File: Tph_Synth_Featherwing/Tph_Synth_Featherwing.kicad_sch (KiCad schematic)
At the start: 3 parts, among them J1 AudioJack3, J2 Conn_01x04

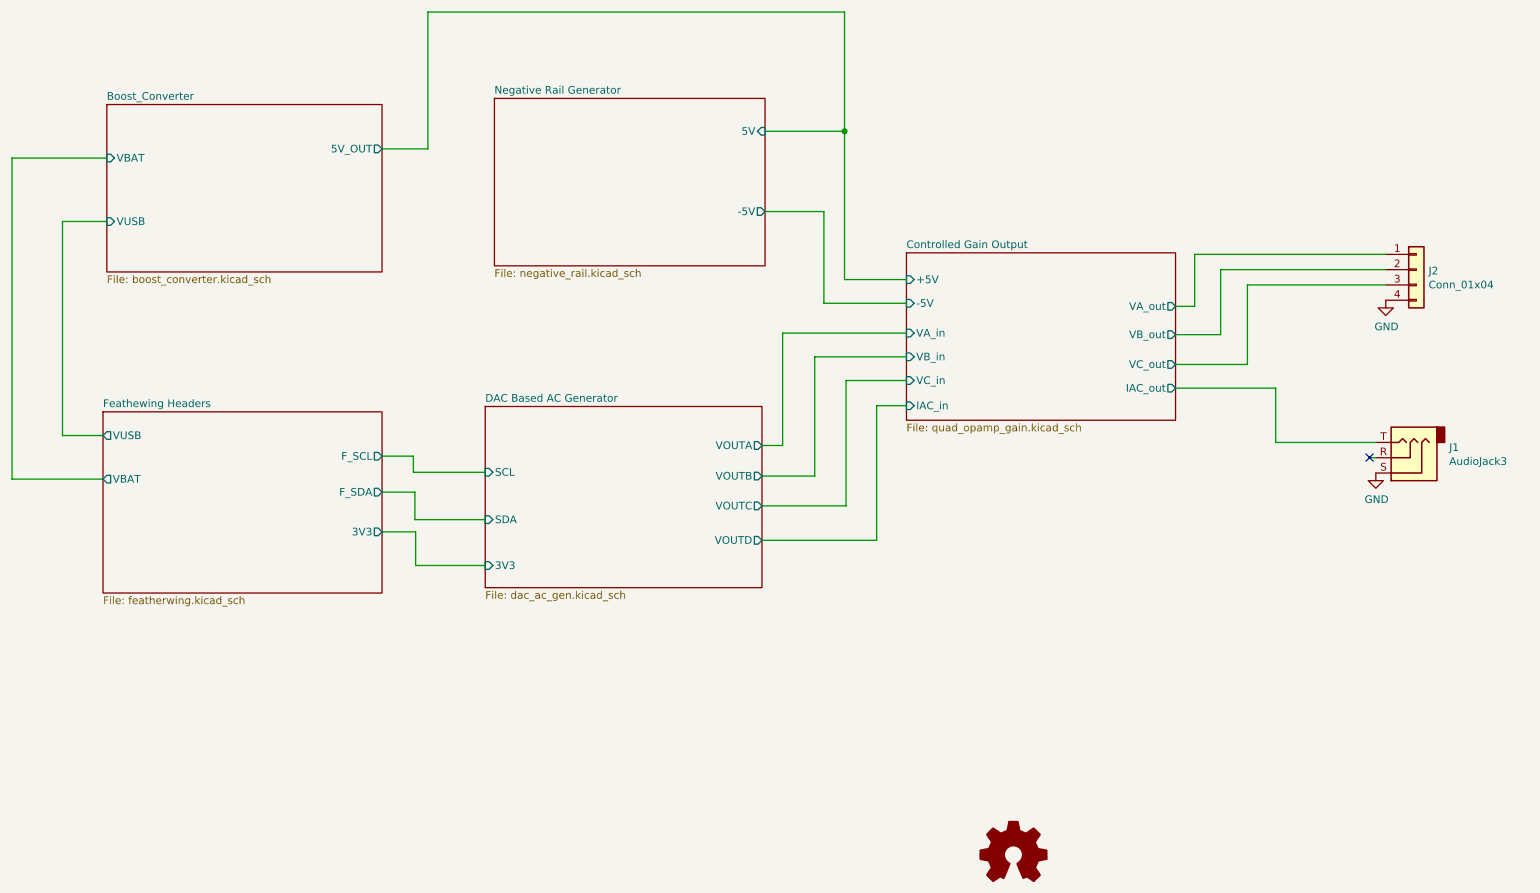
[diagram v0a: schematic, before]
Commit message: Upgrade design to KiCad 10; clear ERC and DRC violations
Co-authored-by: Copilot <223556219+Copilot@users.noreply.github.com>
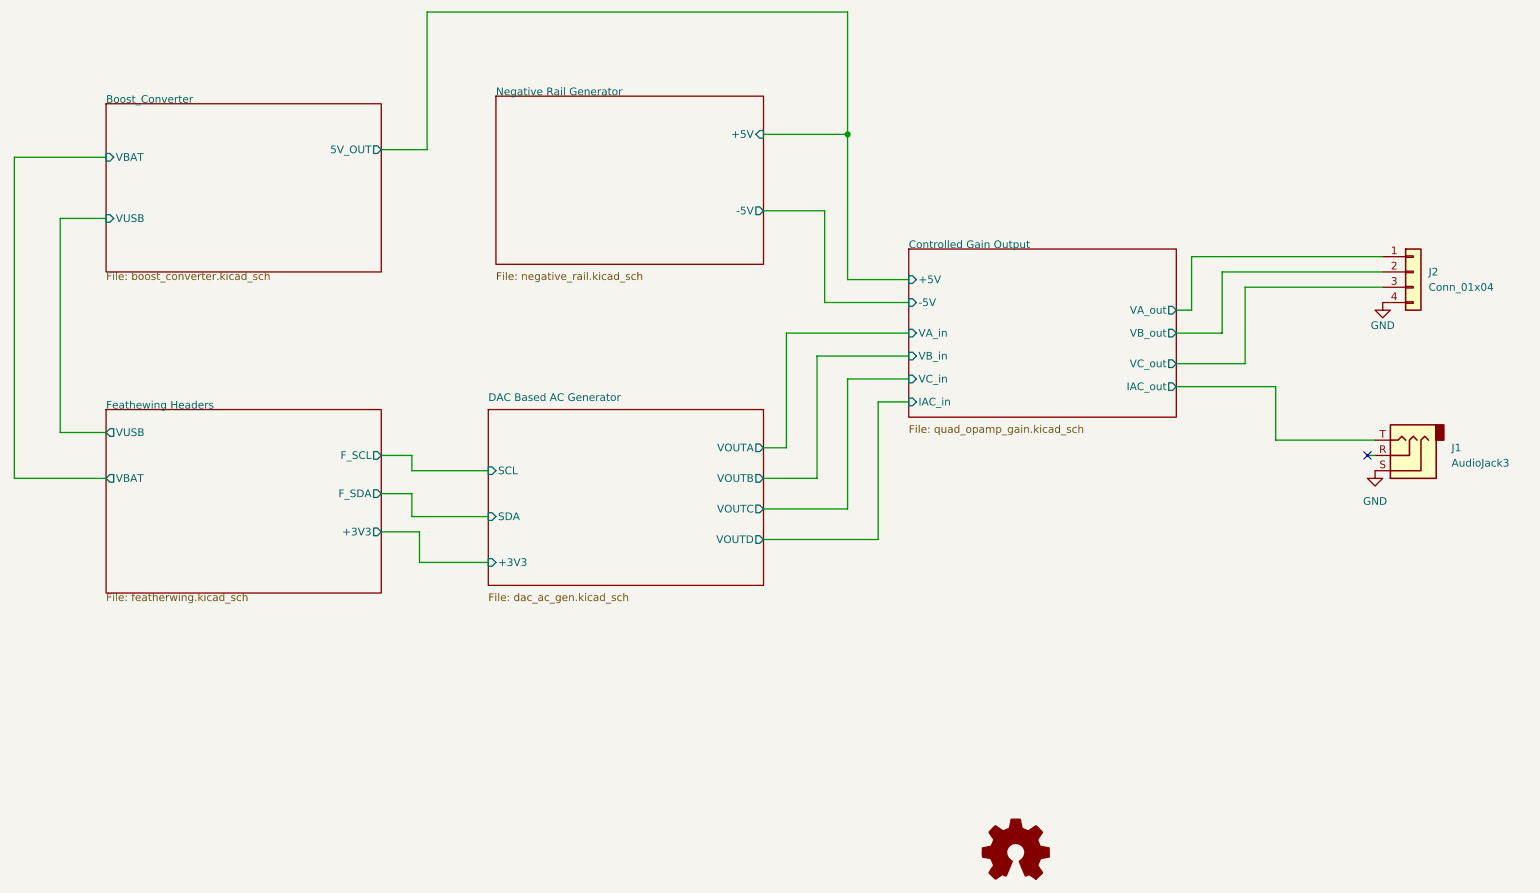
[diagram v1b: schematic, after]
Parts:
- J1: symbol Connector:AudioJack3 -> Connector_Audio:AudioJack3
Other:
- sheet DAC Based AC Generator ports: added +3V3; removed 3V3
- sheet Feathewing Headers ports: added +3V3; removed 3V3
- sheet Negative Rail Generator ports: added +5V; removed 5V
- moved on the sheet: J2

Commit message: Release v0.4 with complete KiCad 10 schematic-PCB parity
Synchronize pad nets, schematic paths, component fields and BOM exclusions while retaining routing and placement. Restore project-local STEP models, fix edge silkscreen using local footprint variants, update revision metadata and improve schematic readability. Include inspected PDF and PCB renders.

Co-authored-by: Copilot <223556219+Copilot@users.noreply.github.com>
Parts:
- J1: footprint Connector_Audio:Jack_3.5mm_CUI_SJ-3523-SMT_Horizontal -> FeatherWing_v04:Jack_3.5mm_CUI_SJ-3523-SMT_Horizontal_EdgeMounted
- J2: footprint Connector_Molex:Molex_Nano-Fit_105314-xx04_2x02_P2.50mm_Horizontal -> FeatherWing_v04:Molex_Nano-Fit_105314-xx04_2x02_P2.50mm_Horizontal_EdgeMounted
- LOGO1: now left out of the parts list
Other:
- title: (none) -> 3-Phase Synth FeatherWing
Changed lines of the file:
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@@
 	(generator_version "10.0")
 	(paper "A4")
+	(title_block
+		(title "3-Phase Synth FeatherWing")
+		(date "2026-10-28")
+		(rev "0.4")
+	)
 	(junction
 		(at 160.02 54.61)
@@
 			)
 		)
-		(property "Footprint" "Connector_Molex:Molex_Nano-Fit_105314-xx04_2x02_P2.50mm_Horizontal"
+		(property "Footprint" "FeatherWing_v04:Molex_Nano-Fit_105314-xx04_2x02_P2.50mm_Horizontal_EdgeMounted"
 			(at 254 77.47 0)
 			(hide yes)
@@
 			)
 		)
-		(property "Footprint" "Connector_Audio:Jack_3.5mm_CUI_SJ-3523-SMT_Horizontal"
+		(property "Footprint" "FeatherWing_v04:Jack_3.5mm_CUI_SJ-3523-SMT_Horizontal_EdgeMounted"
 			(at 252.73 107.95 0)
 			(hide yes)
@@
 		(body_style 1)
 		(exclude_from_sim no)
-		(in_bom yes)
+		(in_bom no)
 		(on_board yes)
 		(in_pos_files yes)
@@
 		)
 	)
+	(sheet_instances
+		(path "/" (page "1"))
+	)
 )
